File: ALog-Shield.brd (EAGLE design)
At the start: 53.3 x 78.5 mm, 27 parts, among them U1 DS3231MZ/V+T

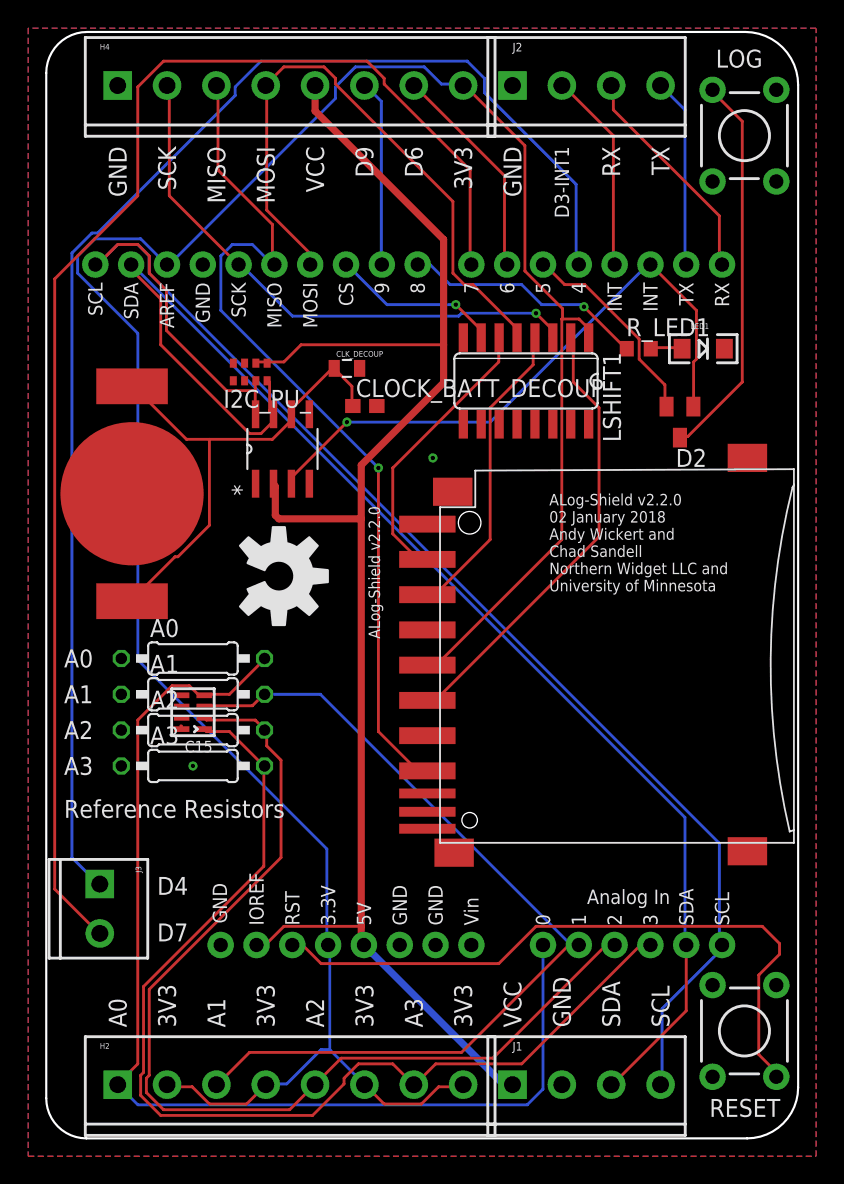
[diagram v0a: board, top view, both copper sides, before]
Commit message: AREF to 3V3 jumper
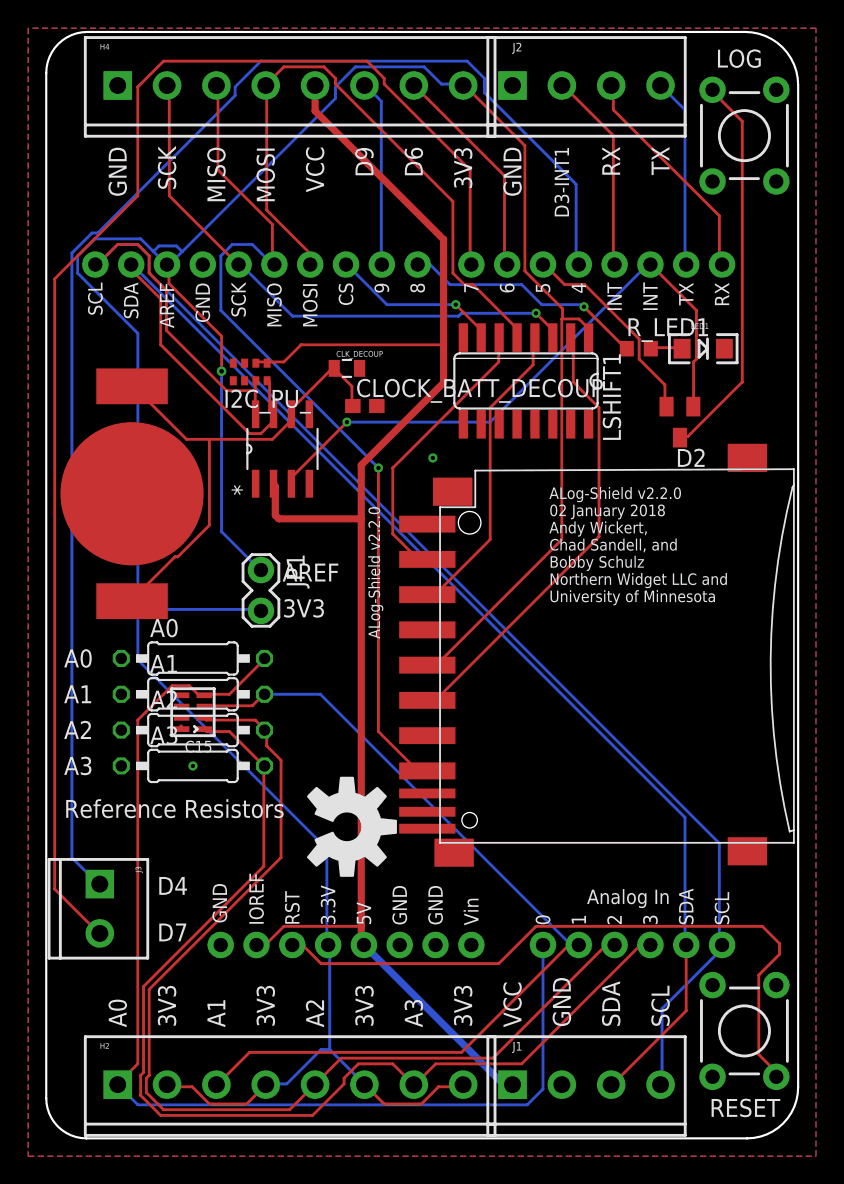
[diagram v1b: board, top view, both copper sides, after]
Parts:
- added JP1: (no value), SparkFun-Connectors:1X02_LOCK
- moved LOGO1 18.4 mm to (21.3, 22.1)
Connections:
- new net AREF: JP1.1, U$9.AREF
- net +3V3: now also JP1.2; no longer U$9.AREF
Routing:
- net AREF: track 0.00 -> 24.5 mm, vias 0 -> 1
- net +3V3: track 175.7 -> 186.7 mm
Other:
- board text added: "ALog-Shield v2.2.0 02 January 2018 Andy Wickert, Chad Sandell, and Bobby Schulz Northern Widget LLC and University of Minnesota"
- board text added: "AREF"
- board text removed: "ALog-Shield v2.2.0 02 January 2018 Andy Wickert and Chad Sandell Northern Widget LLC and University of Minnesota"
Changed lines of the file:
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@@
 <text x="23.6855" y="35.433" size="0.8128" layer="21" rot="R90">ALog-Shield v2.2.0</text>
 <text x="1.27" y="22.733" size="1.27" layer="21">Reference Resistors</text>
-<text x="35.687" y="38.7985" size="0.8128" layer="21">ALog-Shield v2.2.0
+<text x="35.687" y="38.0365" size="0.8128" layer="21">ALog-Shield v2.2.0
 02 January 2018
-Andy Wickert and
-Chad Sandell
+Andy Wickert,
+Chad Sandell, and
+Bobby Schulz
 Northern Widget LLC and
 University of Minnesota</text>
@@
 Northern Widget LLC</text>
 <text x="3.81" y="69.596" size="0.6096" layer="22" rot="MR0">TM</text>
+<text x="16.764" y="39.497" size="1.27" layer="21">AREF</text>
+<text x="16.764" y="36.957" size="1.27" layer="21">3V3</text>
 </plain>
 <attributes>
@@
 <element name="U$2" library="awickert" package="MADE_IN_MN_SHIELD_220" value="MADE_IN_MN_220_SHIELD" x="42.926" y="30.48" rot="R90"/>
 <element name="U$3" library="awickert" package="ALOG_LOG" value="ALOG_LOG" x="19.558" y="35.052" rot="R90"/>
-<element name="LOGO1" library="SparkFun-Aesthetics" package="OSHW-LOGO-L" value="OSHW-LOGOL" x="16.51" y="39.878" rot="R270"/>
+<element name="LOGO1" library="SparkFun-Aesthetics" package="OSHW-LOGO-L" value="OSHW-LOGOL" x="21.336" y="22.098" rot="R270"/>
 <element name="J3" library="SparkFun-Connectors" package="SCREWTERMINAL-3.5MM-2" value="" x="3.81" y="18.034" rot="R270">
 <attribute name="PROD_ID" value="CONN-08399" x="3.81" y="18.034" size="1.778" layer="27" rot="R270" display="off"/>
@@
 <element name="U$1" library="awickert" package="NWLOGO_MED" value="NWLOGO_MED" x="7.874" y="67.818" rot="MR0"/>
 <element name="CLK_DECOUP" library="SparkFun-Passives" package="0805" value="10 uF" x="21.336" y="54.61"/>
+<element name="JP1" library="SparkFun-Connectors" package="1X02_LOCK" value="" x="15.24" y="40.132" rot="R270"/>
 </elements>
 <signals>
@@
 </signal>
 <signal name="+3V3">
-<contactref element="U$9" pad="AREF"/>
 <contactref element="U$9" pad="3.3V"/>
 <contactref element="H2" pad="2"/>
@@
 <wire x1="19.9136" y1="20.5232" x2="19.9136" y2="13.8176" width="0.2032" layer="16"/>
 <wire x1="6.5024" y1="33.9344" x2="19.9136" y2="20.5232" width="0.2032" layer="16"/>
-<wire x1="6.5024" y1="57.0992" x2="6.5024" y2="33.9344" width="0.2032" layer="16"/>
+<wire x1="6.5024" y1="57.0992" x2="6.5024" y2="37.5158" width="0.2032" layer="16"/>
+<wire x1="6.5024" y1="37.5158" x2="6.5024" y2="33.9344" width="0.2032" layer="16"/>
 <wire x1="2.2352" y1="61.3664" x2="6.5024" y2="57.0992" width="0.2032" layer="16"/>
 <wire x1="2.2352" y1="62.5856" x2="2.2352" y2="61.3664" width="0.2032" layer="16"/>
 <wire x1="3.4544" y1="63.8048" x2="2.2352" y2="62.5856" width="0.2032" layer="16"/>
 <wire x1="6.7056" y1="63.8048" x2="3.4544" y2="63.8048" width="0.2032" layer="16"/>
-<wire x1="8.5344" y1="61.976" x2="6.7056" y2="63.8048" width="0.2032" layer="16"/>
+<wire x1="8.5344" y1="61.976" x2="7.6073" y2="62.9031" width="0.2032" layer="16"/>
+<wire x1="7.6073" y1="62.9031" x2="6.7056" y2="63.8048" width="0.2032" layer="16"/>
 <wire x1="19.9136" y1="13.8176" x2="20.0025" y2="13.716" width="0.2032" layer="16"/>
-<wire x1="8.5344" y1="61.976" x2="8.5725" y2="61.976" width="0.2032" layer="16"/>
 <wire x1="28.0416" y1="74.7776" x2="29.464" y2="74.7776" width="0.2032" layer="16"/>
 <wire x1="26.8224" y1="75.9968" x2="28.0416" y2="74.7776" width="0.2032" layer="16"/>
@@
 <wire x1="20.5232" y1="74.5744" x2="21.9456" y2="75.9968" width="0.2032" layer="16"/>
 <wire x1="20.5232" y1="73.7616" x2="20.5232" y2="74.5744" width="0.2032" layer="16"/>
-<wire x1="8.7376" y1="61.976" x2="20.5232" y2="73.7616" width="0.2032" layer="16"/>
+<wire x1="8.7376" y1="61.976" x2="9.652" y2="62.8904" width="0.2032" layer="16"/>
+<wire x1="9.652" y1="62.8904" x2="20.5232" y2="73.7616" width="0.2032" layer="16"/>
 <wire x1="29.464" y1="74.7776" x2="29.58" y2="74.676" width="0.2032" layer="16"/>
-<wire x1="8.7376" y1="61.976" x2="8.5725" y2="61.976" width="0.2032" layer="16"/>
 <contactref element="LSHIFT1" pad="1"/>
 <contactref element="SD1" pad="4"/>
@@
 <wire x1="36.6268" y1="58.1406" x2="36.576" y2="58.1152" width="0.2032" layer="1"/>
 <wire x1="29.6926" y1="74.676" x2="29.58" y2="74.676" width="0.2032" layer="1"/>
+<contactref element="JP1" pad="2"/>
+<wire x1="6.5024" y1="37.5158" x2="15.113" y2="37.5158" width="0.2032" layer="16"/>
+<wire x1="15.113" y1="37.5158" x2="15.24" y2="37.4142" width="0.2032" layer="16"/>
+<wire x1="8.001" y1="63.2968" x2="7.6073" y2="62.9031" width="0.2032" layer="16"/>
+<wire x1="9.2456" y1="63.2968" x2="8.001" y2="63.2968" width="0.2032" layer="16"/>
+<wire x1="9.652" y1="62.8904" x2="9.2456" y2="63.2968" width="0.2032" layer="16"/>
 </signal>
 <signal name="SCL">
@@
 <contactref element="U$9" pad="VIN"/>
 </signal>
+<signal name="AREF">
+<contactref element="U$9" pad="AREF"/>
+<contactref element="JP1" pad="1"/>
+<wire x1="8.7122" y1="60.6298" x2="8.7122" y2="61.8744" width="0.2032" layer="1"/>
+<wire x1="12.446" y1="56.896" x2="8.7122" y2="60.6298" width="0.2032" layer="1"/>
+<wire x1="12.446" y1="54.4068" x2="12.446" y2="56.896" width="0.2032" layer="1"/>
+<wire x1="12.446" y1="43.0276" x2="12.446" y2="54.4068" width="0.2032" layer="16"/>
+<wire x1="15.113" y1="40.3606" x2="12.446" y2="43.0276" width="0.2032" layer="16"/>
+<wire x1="8.7122" y1="61.8744" x2="8.5725" y2="61.976" width="0.2032" layer="1"/>
+<wire x1="15.113" y1="40.3606" x2="15.24" y2="40.3098" width="0.2032" layer="16"/>
+<via x="12.446" y="54.4068" extent="1-16" drill="0.3302"/>
+</signal>
 </signals>

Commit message: New buttons: consistent with TLog
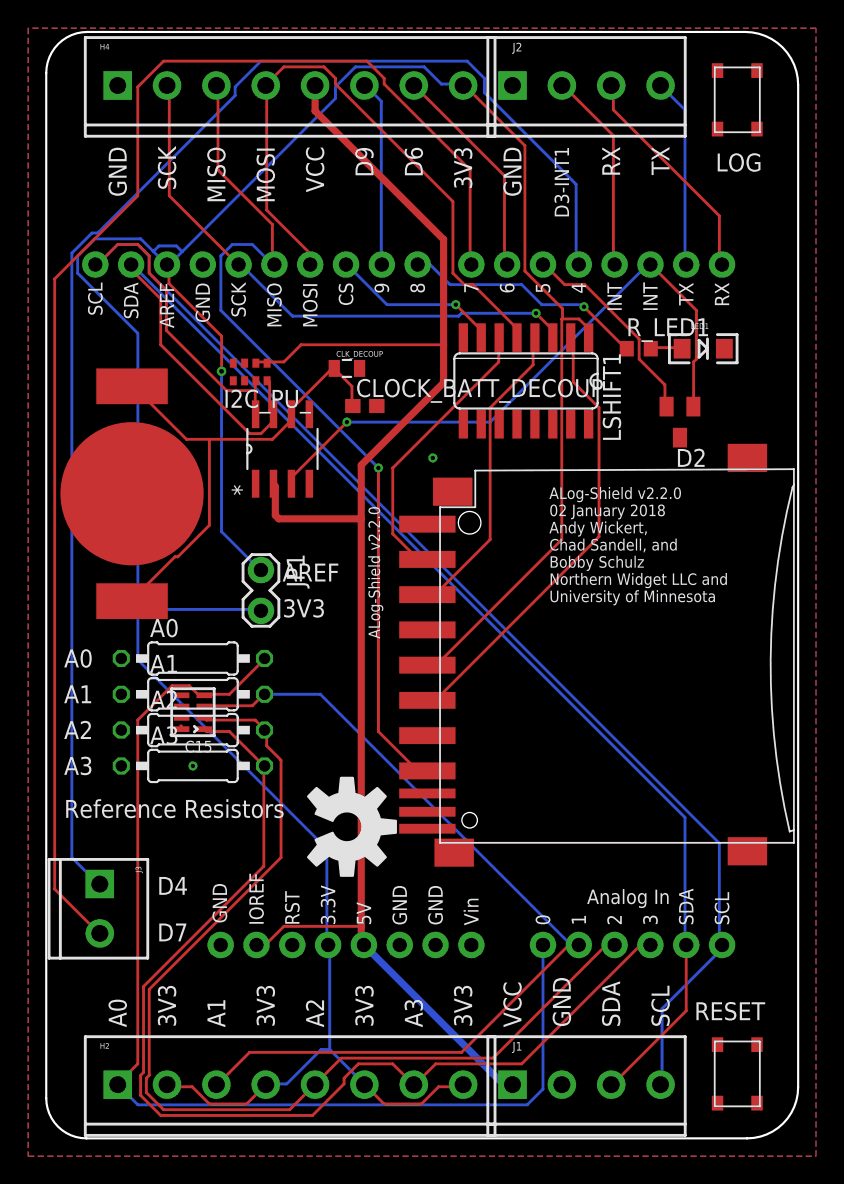
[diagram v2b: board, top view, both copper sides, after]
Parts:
- LOG, RESET: device SparkFun-Electromechanical:TACTILE-PTH -> bschulz:SWITCH_4.2X3.2
- moved RESET 3.09 mm to (49.0, 4.57)
- moved LOG 2.59 mm to (49.0, 73.7)
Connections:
- net N$11: now also LOG.2; no longer LOG.3
- net RESET: now also RESET.2; no longer RESET.3
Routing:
- net RESET: track 47.6 -> 0.00 mm
- net N$11: track 27.6 -> 0.00 mm
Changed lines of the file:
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@@
 <element name="R_LED1" library="resistor" package="R0603" value="220" x="42.037" y="56.007"/>
 <element name="A1" library="resistor" package="0207/10" value="" x="10.414" y="31.496"/>
-<element name="RESET" library="SparkFun-Electromechanical" package="TACTILE-PTH" value="Reset" x="49.53" y="7.62" smashed="yes" rot="R90">
-<attribute name="NAME" x="52.07" y="2.794" size="1.27" layer="21" ratio="10" rot="R180"/>
-<attribute name="PROD_ID" value=" SWCH-08441" x="218.44" y="-81.28" size="1.778" layer="27" rot="R90" display="off"/>
+<element name="RESET" library="bschulz" package="SWITCH_4.2X3.2" value="Reset" x="49.022" y="4.572" smashed="yes" rot="R90">
+<attribute name="NAME" x="45.974" y="8.382" size="1.27" layer="21" ratio="10"/>
 </element>
 <element name="CLOCK_BATT_DECOUP" library="rcl" package="C0603" value="0.1uF" x="22.606" y="51.943"/>
@@
 <attribute name="VALUE" x="46.863" y="53.975" size="1.27" layer="27" rot="R180"/>
 </element>
-<element name="LOG" library="SparkFun-Electromechanical" package="TACTILE-PTH" value="LOG" x="49.53" y="71.12" smashed="yes" rot="R270">
-<attribute name="NAME" x="47.498" y="75.946" size="1.27" layer="21" ratio="10"/>
-<attribute name="PROD_ID" value=" SWCH-08441" x="-179.705" y="172.72" size="1.778" layer="27" rot="R270" display="off"/>
+<element name="LOG" library="bschulz" package="SWITCH_4.2X3.2" value="LOG" x="49.022" y="73.66" smashed="yes" rot="R270">
+<attribute name="NAME" x="50.8" y="69.85" size="1.27" layer="21" ratio="10" rot="R180"/>
 </element>
 <element name="U1" library="Maxim-DS3231MZ_8-SOIC" package="21-0041B_8" value="DS3231MZ/V+T" x="16.764" y="48.895" rot="R90">
@@
 <signal name="RESET">
 <contactref element="U$9" pad="RES"/>
-<contactref element="RESET" pad="3"/>
-<wire x1="52.0192" y1="13.0556" x2="52.0192" y2="13.8176" width="0.2032" layer="1"/>
-<wire x1="50.546" y1="11.5824" x2="52.0192" y2="13.0556" width="0.2032" layer="1"/>
-<wire x1="50.546" y1="5.9436" x2="50.546" y2="11.5824" width="0.2032" layer="1"/>
-<wire x1="52.0192" y1="4.4704" x2="50.546" y2="5.9436" width="0.2032" layer="1"/>
-<wire x1="52.0192" y1="4.4704" x2="51.7906" y2="4.3688" width="0.2032" layer="1"/>
-<wire x1="18.288" y1="13.6144" x2="17.4752" y2="13.6144" width="0.2032" layer="1"/>
-<wire x1="19.5072" y1="12.3952" x2="18.288" y2="13.6144" width="0.2032" layer="1"/>
-<wire x1="32.1056" y1="12.3952" x2="19.5072" y2="12.3952" width="0.2032" layer="1"/>
-<wire x1="34.7472" y1="15.0368" x2="32.1056" y2="12.3952" width="0.2032" layer="1"/>
-<wire x1="50.8" y1="15.0368" x2="34.7472" y2="15.0368" width="0.2032" layer="1"/>
-<wire x1="52.0192" y1="13.8176" x2="50.8" y2="15.0368" width="0.2032" layer="1"/>
-<wire x1="17.4752" y1="13.6144" x2="17.4625" y2="13.716" width="0.2032" layer="1"/>
+<contactref element="RESET" pad="2"/>
+<wire x1="17.4625" y1="13.716" x2="47.622" y2="6.647" width="0" layer="19" extent="1-1"/>
 </signal>
 <signal name="A2">
@@
 </signal>
 <signal name="N$11">
-<contactref element="LOG" pad="3"/>
+<contactref element="LOG" pad="2"/>
 <contactref element="D2" pad="3"/>
-<wire x1="45.5168" y1="49.784" x2="45.1104" y2="49.784" width="0.2032" layer="1"/>
-<wire x1="49.3776" y1="53.6448" x2="45.5168" y2="49.784" width="0.2032" layer="1"/>
-<wire x1="49.3776" y1="72.136" x2="49.3776" y2="53.6448" width="0.2032" layer="1"/>
-<wire x1="47.5488" y1="73.9648" x2="49.3776" y2="72.136" width="0.2032" layer="1"/>
-<wire x1="45.1104" y1="49.784" x2="44.958" y2="49.7" width="0.2032" layer="1"/>
-<wire x1="47.5488" y1="73.9648" x2="47.2694" y2="74.3712" width="0.2032" layer="1"/>
+<wire x1="44.958" y1="49.7" x2="50.422" y2="71.585" width="0" layer="19" extent="1-1"/>
 </signal>
 <signal name="D4">
